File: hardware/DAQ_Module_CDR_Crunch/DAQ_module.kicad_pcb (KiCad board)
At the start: 2 copper layers, 53 parts, among them J1 Conn_01x10_Pin, J2 Conn_01x10_Pin, J3 Conn_01x10_Pin, U1 MCP3564RT-E/ST, U2 MAX31855KASA, U3 MAX31855KASA, U5 TPS70933DBVR, U6 TPS70933DBVR, U7 TPS70933DBVR, U8 MAX31855KASA

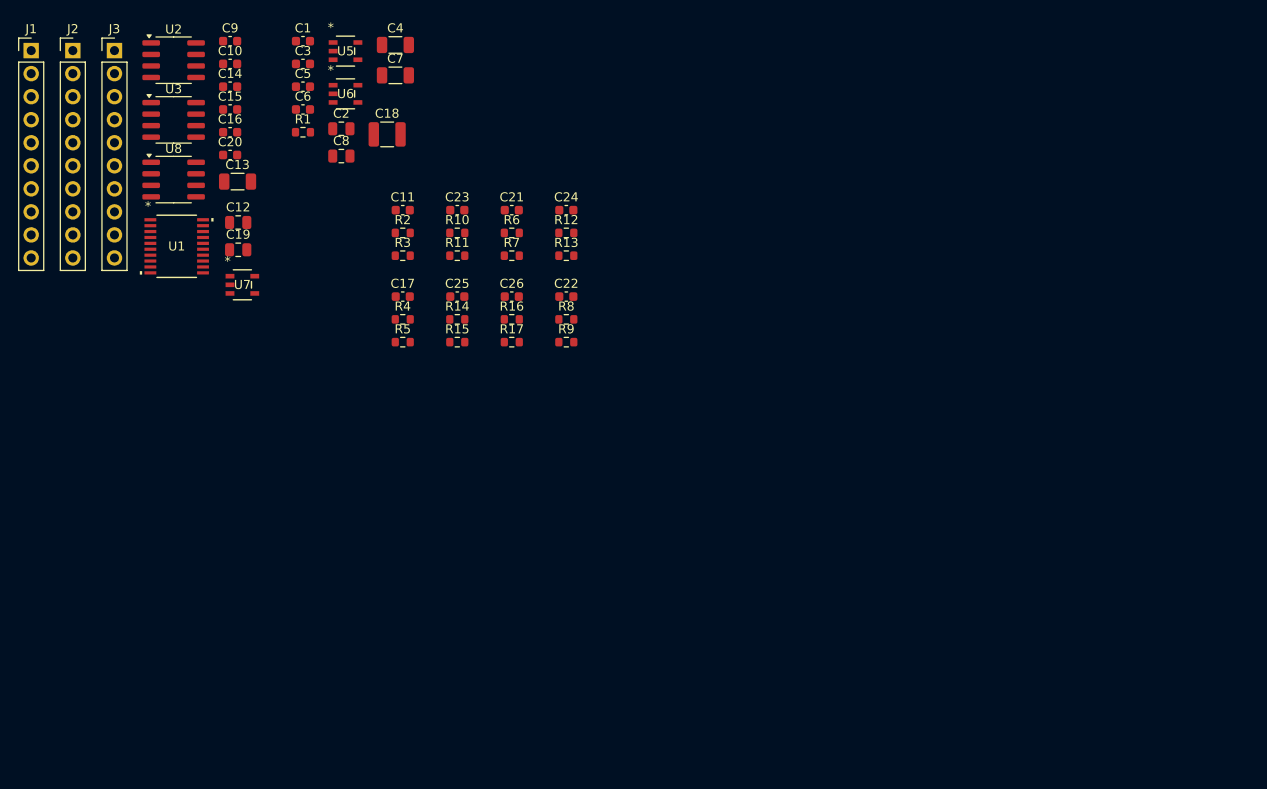
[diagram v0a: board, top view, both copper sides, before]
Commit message: Ready for final review. Added downloadable footprint and symbol of board
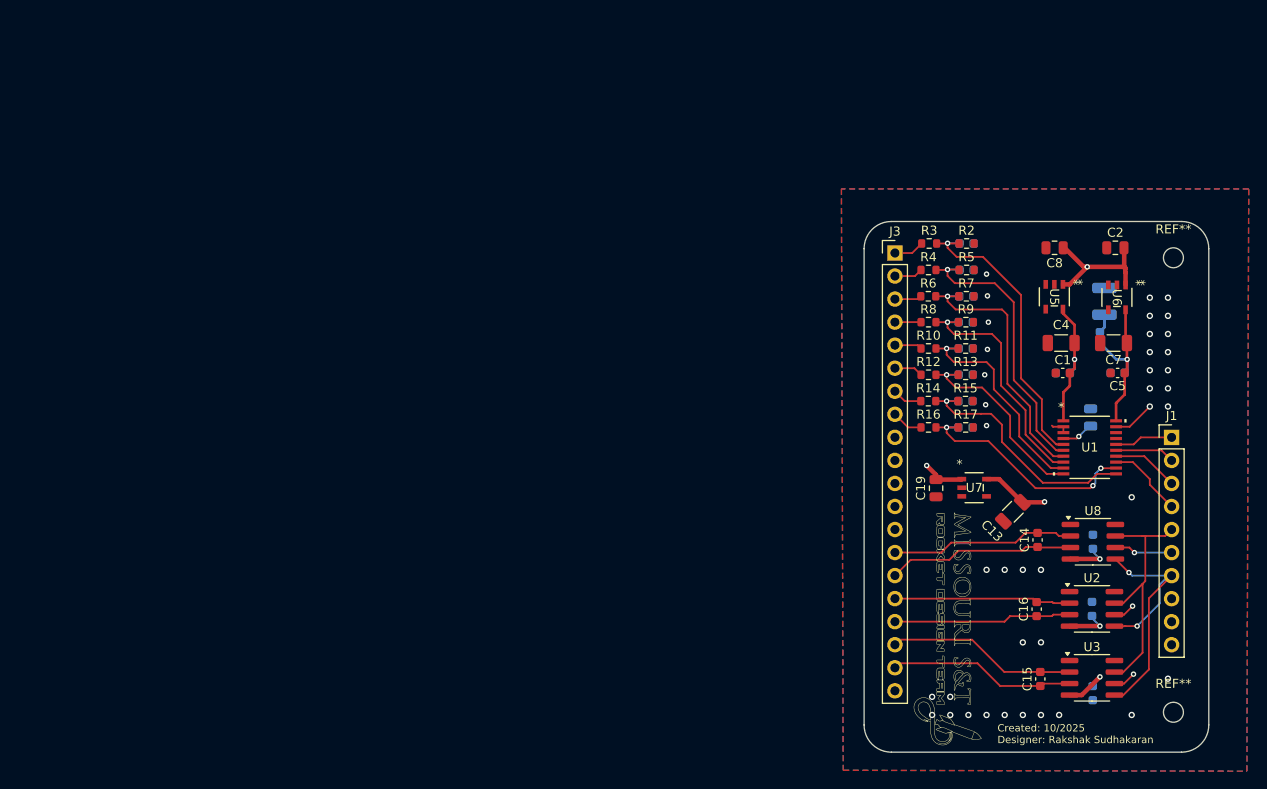
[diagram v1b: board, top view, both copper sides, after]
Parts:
- removed J2: Conn_01x10_Pin, Connector_PinHeader_2.54mm:PinHeader_1x10_P2.54mm_Vertical
- added G***: LOGO, RDT_Logo:RDT_Logo, F.Cu at (169.2, 109.6)
- added REF**: MountingHole_2.2mm_M2, MountingHole:MountingHole_2.2mm_M2, F.Cu at (194.1, 118.8)
- added REF**: MountingHole_2.2mm_M2, MountingHole:MountingHole_2.2mm_M2, F.Cu at (194.1, 68.7)
- C10, C11, C12, C17, C18, C20, C21, C22, C23, C24, C25, C26, C3, C6, C9, R1: moved to B.Cu
- J3: value Conn_01x10_Pin -> Conn_01x20_Pin; footprint Connector_PinHeader_2.54mm:PinHeader_1x10_P2.54mm_Vertical -> Connector_PinHeader_2.54mm:PinHeader_1x20_P2.54mm_Vertical
- moved J1 132.7 mm to (193.9, 88.5)
- moved C9 119.2 mm to (185.2, 116.7), turned to -90 degrees
- moved U3 118.5 mm to (185.1, 115.0)
- moved U2 117.9 mm to (185.1, 107.4)
- moved C10 112.4 mm to (185.1, 107.4), turned to 90 degrees
- moved C15 109.2 mm to (179.4, 115.1), turned to 90 degrees
- moved U8 108.9 mm to (185.2, 100.0)
- moved C20 104.2 mm to (185.2, 100.0), turned to 90 degrees
- moved C16 103.3 mm to (179.0, 107.4), turned to 90 degrees
- moved U1 103.1 mm to (184.9, 89.6)
- moved C14 102.1 mm to (179.1, 99.8), turned to 90 degrees
- moved C12 96.4 mm to (185.0, 86.3), turned to -90 degrees
- moved C5 95.2 mm to (187.9, 81.4), turned to 180 degrees
- moved C6 94.4 mm to (187.9, 81.4), turned to 180 degrees
- moved C13 92.9 mm to (176.4, 96.7), turned to -135 degrees
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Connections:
- C19 pad 1: Net-(U7-GND) -> GND
- C2 pad 1: Net-(U5-GND) -> GND
- C8 pad 2: Net-(U6-GND) -> GND
- J1 pad 2: /GPIO5 (CS_ADC) -> /GPIO7 (MOSI_ADC)
- J1 pad 4: /GPIO7 (MOSI_ADC) -> /GPIO5 (CS_ADC)
- J1 pad 8: /GPIO12 (CS_N20) -> /GPIO13 (CS Chamber Shell_2)
- J1 pad 9: /GPIO13 (CS Chamber Shell_2) -> /GPIO12 (CS_N20)
- J3 pad 1: /T+ (Chamber Shell_1) -> /ADC_AI0
- J3 pad 2: /T- (Chamber Shell_1) -> /ADC_AI1
- J3 pad 3: /T+ (Chamber Shell_2) -> /ADC_AI2
- J3 pad 4: /T- (Chamber Shell_2) -> /ADC_AI3
- J3 pad 5: /T+ (N2O) -> /ADC_AI4
- J3 pad 6: /T- (N2O) -> /ADC_AI5
- J3 pad 7: +5V -> /ADC_AI6
- J3 pad 8: GND -> /ADC_AI7
- U5 pad 2: Net-(U5-GND) -> GND
- U6 pad 2: Net-(U6-GND) -> GND
- U7 pad 2: Net-(U7-GND) -> GND
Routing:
- net +5V: track 0.00 -> 60.7 mm, vias 0 -> 2
- net Net-(U2-V_{CC}): track 0.00 -> 46.8 mm, vias 0 -> 4
- net /ADC_AI_Filt_0: track 0.00 -> 33.5 mm, vias 0 -> 1
- net /GPIO10 (SCK_TCIC): track 0.00 -> 33.1 mm, vias 0 -> 2
- net /ADC_AI_Filt_1: track 0.00 -> 32.2 mm, vias 0 -> 1
- net /ADC_AI_Filt_2: track 0.00 -> 30.5 mm, vias 0 -> 1
- net /ADC_AI_Filt_6: track 0.00 -> 28.0 mm, vias 0 -> 1
- net /GPIO8 (MISO_TCIC): track 0.00 -> 27.8 mm
- net /ADC_AI_Filt_3: track 0.00 -> 27.7 mm, vias 0 -> 1
- net /ADC_AI_Filt_7: track 0.00 -> 27.1 mm, vias 0 -> 3
- net /ADC_AI_Filt_4: track 0.00 -> 25.2 mm, vias 0 -> 1
- net /ADC_AI_Filt_5: track 0.00 -> 22.8 mm, vias 0 -> 1
- net /T- (N2O): track 0.00 -> 21.0 mm
- net /T+ (Chamber Shell_1): track 0.00 -> 20.7 mm
- net /T+ (N2O): track 0.00 -> 20.6 mm
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- added copper zone on B.Cu, net GND
- added copper zone on F.Cu, net GND
- added copper zone on In1.Cu, net GND
- added copper zone on In2.Cu, net GND
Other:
- board outline added: 38 x 58.5 mm
- copper layers 2 -> 4
- board text added: "Created: 10/2025 Designer: Rakshak Sudhakaran"
- board text added: "{ "ViaStitching": "0.2", "stitch_zone_0": { "HSpacing": "1", "VSpacing": "1", "HOffset": "0", "VOffset": "0", "Clearance": "0", "Randomize": false } }"
- board text added: "{ "ViaStitching": "0.2", "stitch_zone_0": { "HSpacing": "1", "VSpacing": "1", "HOffset": "0", "VOffset": "0", "Clearance": "1", "Randomize": false } }"
- board text added: "{ "ViaStitching": "0.2", "stitch_zone_0": { "HSpacing": "1.5", "VSpacing": "1.5", "HOffset": "0", "VOffset": "0", "Clearance": "1.5", "Randomize": false } }"
- board text added: "{ "ViaStitching": "0.2", "stitch_zone_0": { "HSpacing": "2", "VSpacing": "2", "HOffset": "0", "VOffset": "0", "Clearance": "1.5", "Randomize": false } }"
- board text added: "{ "ViaStitching": "0.2", "stitch_zone_0": { "HSpacing": "2", "VSpacing": "2", "HOffset": "0", "VOffset": "0", "Clearance": "1.7", "Randomize": false } }"
- board text added: "{ "ViaStitching": "0.2", "stitch_zone_0": { "HSpacing": "2", "VSpacing": "2", "HOffset": "0", "VOffset": "0", "Clearance": "2", "Randomize": false } }"
- board text added: "{ "ViaStitching": "0.2", "stitch_zone_0": { "HSpacing": "2.5", "VSpacing": "2.5", "HOffset": "0", "VOffset": "0", "Clearance": "2.5", "Randomize": false } }"
- board text added: "{ "ViaStitching": "0.2", "stitch_zone_0": { "HSpacing": "3", "VSpacing": "3", "HOffset": "0", "VOffset": "0", "Clearance": "3", "Randomize": false } }"
- board text added: "{ "ViaStitching": "0.2", "stitch_zone_0": { "HSpacing": "5", "VSpacing": "5", "HOffset": "0", "VOffset": "0", "Clearance": "5", "Randomize": false } }"

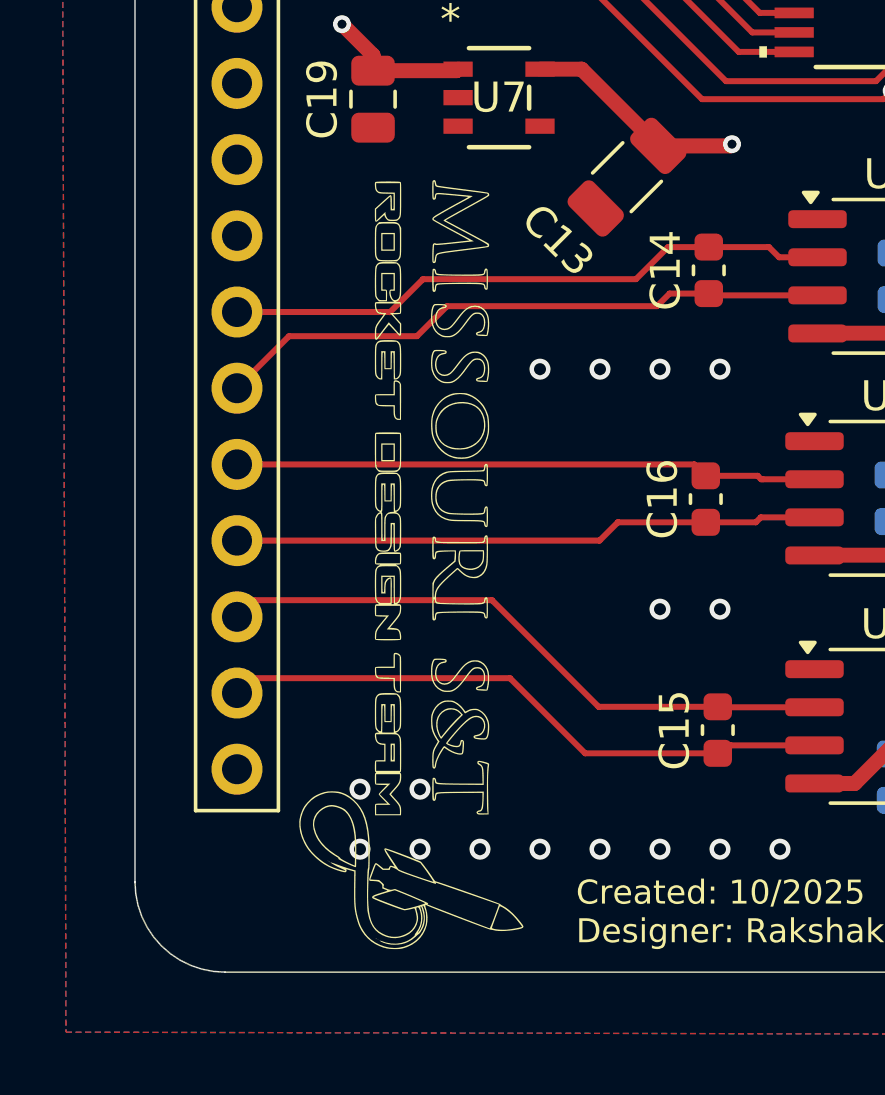
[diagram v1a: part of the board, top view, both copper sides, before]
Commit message: Fixed logo and mounting holes
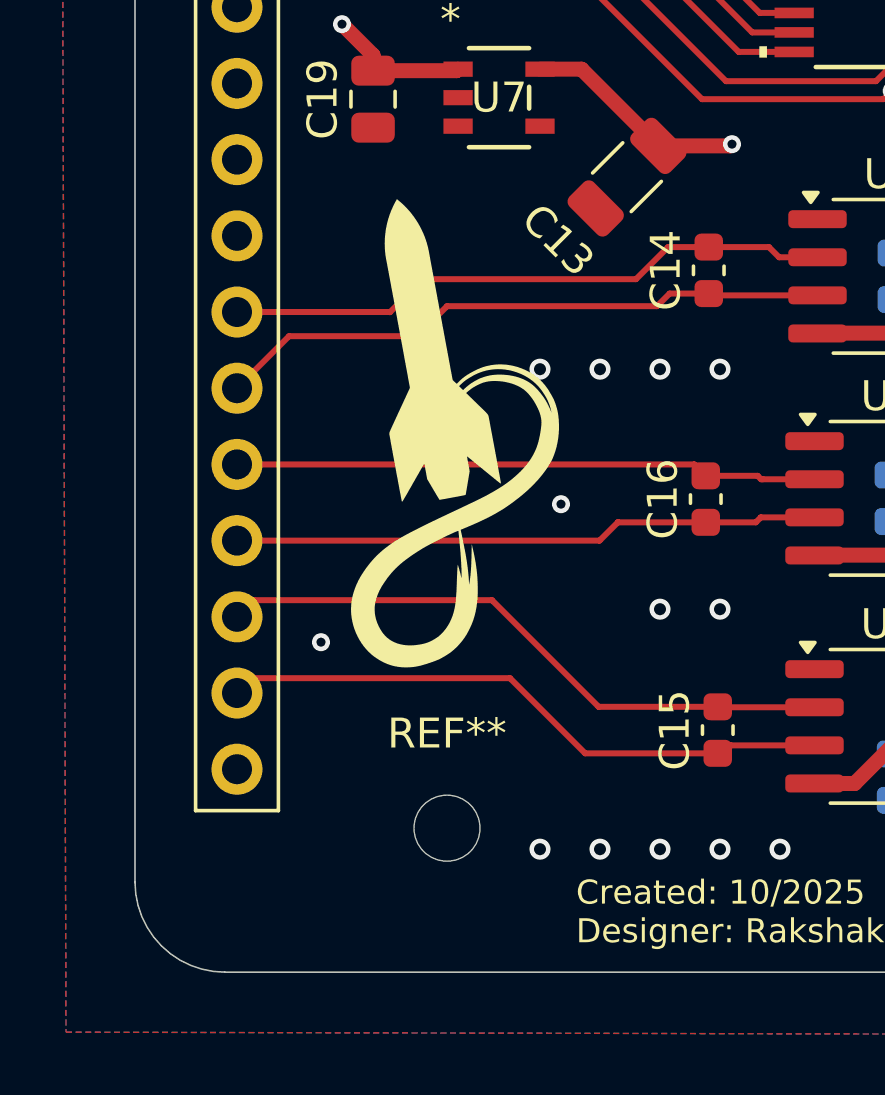
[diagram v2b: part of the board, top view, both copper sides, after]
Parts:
- added REF**: MountingHole_2.2mm_M2, MountingHole:MountingHole_2.2mm_M2, F.Cu at (170.4, 118.4)
- moved G*** 4.30 mm to (169.1, 105.3), turned to 30 degrees
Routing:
- net GND: vias 40 -> 37

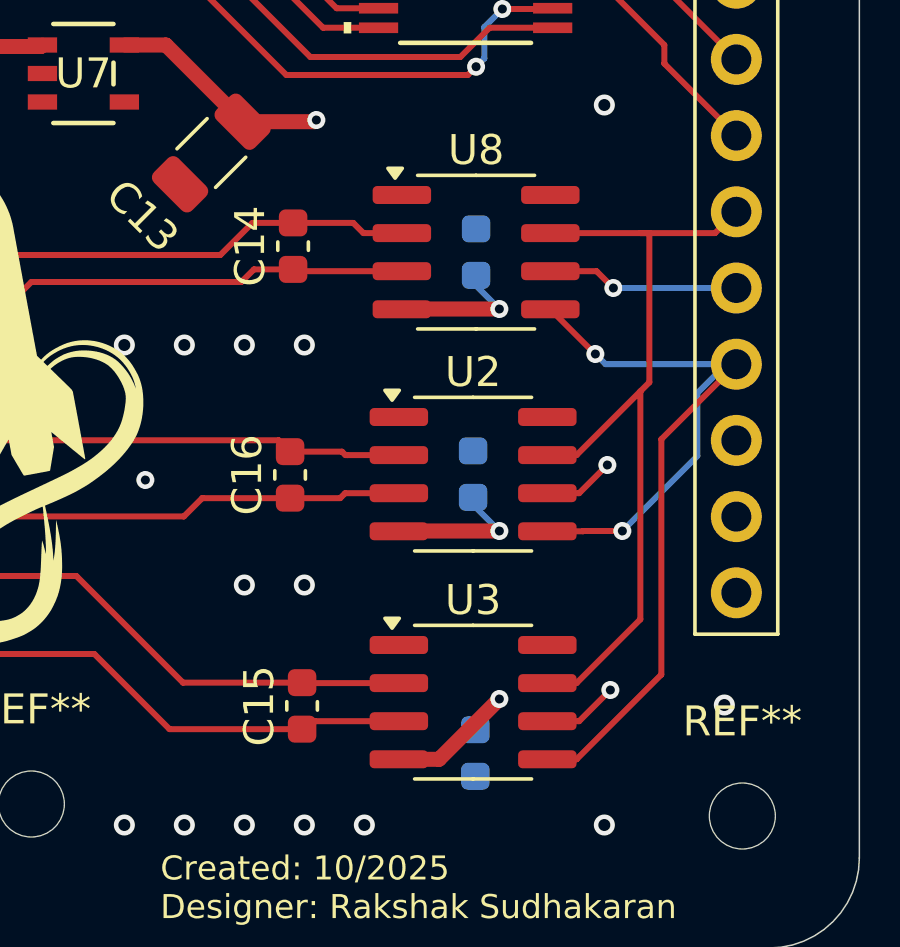
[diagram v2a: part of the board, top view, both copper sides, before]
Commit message: Improved some via spacing
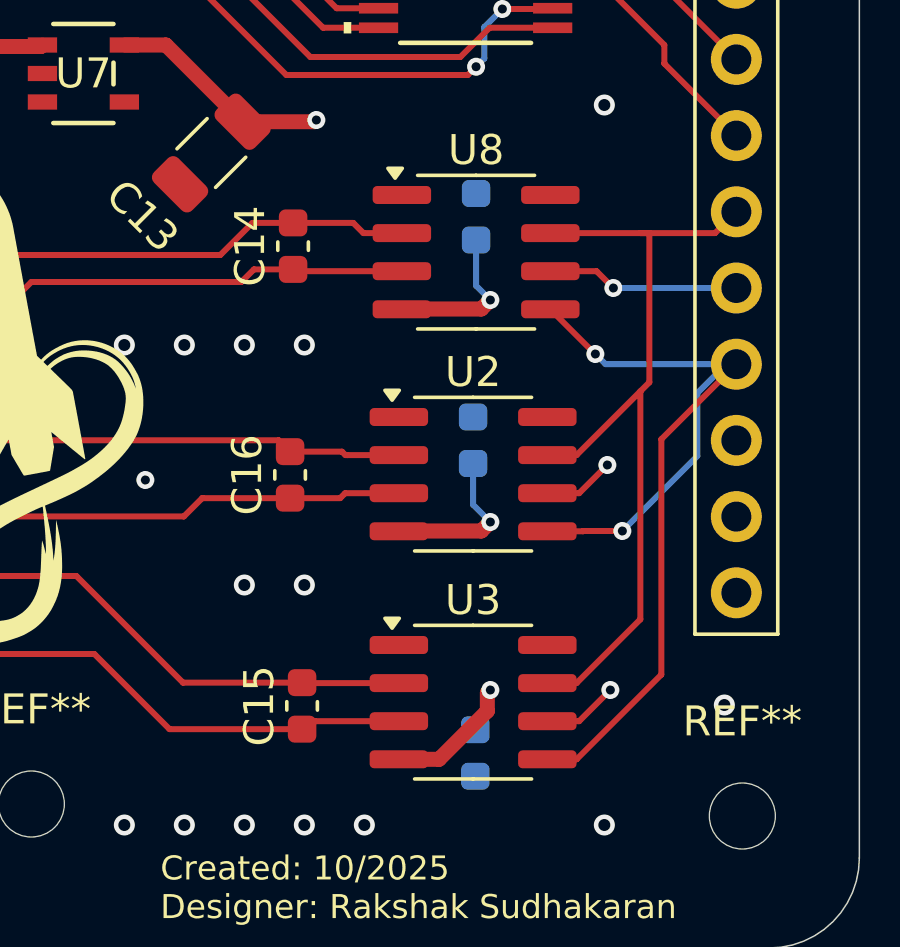
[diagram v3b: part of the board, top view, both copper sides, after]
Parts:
- moved C20 1.18 mm to (185.2, 98.8)
- moved C10 1.13 mm to (185.1, 106.3)
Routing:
- net Net-(U2-V_{CC}): track 46.8 -> 47.9 mm
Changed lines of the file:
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@@
 	(footprint "Capacitor_SMD:C_0603_1608Metric"
 		(layer "B.Cu")
-		(at 185.225 100.005 90)
+		(at 185.225 98.825 90)
 		(descr "Capacitor SMD 0603 (1608 Metric), square (rectangular) end terminal, IPC-7351 nominal, (Body size source: IPC-SM-782 page 76, https://www.pcb-3d.com/wordpress/wp-content/uploads/ipc-sm-782a_amendment_1_and_2.pdf), generated with kicad-footprint-generator")
 		(tags "capacitor")
@@
 	(footprint "Capacitor_SMD:C_0603_1608Metric"
 		(layer "B.Cu")
-		(at 185.125 107.405 90)
+		(at 185.125 106.275 90)
 		(descr "Capacitor SMD 0603 (1608 Metric), square (rectangular) end terminal, IPC-7351 nominal, (Body size source: IPC-SM-782 page 76, https://www.pcb-3d.com/wordpress/wp-content/uploads/ipc-sm-782a_amendment_1_and_2.pdf), generated with kicad-footprint-generator")
 		(tags "capacitor")
@@
 	)
 	(segment
-		(start 186 109.3)
-		(end 182.66 109.3)
+		(start 182.66 109.3)
+		(end 182.65 109.31)
 		(width 0.5)
 		(layer "F.Cu")
@@
 	)
 	(segment
+		(start 185.6 115.3)
+		(end 183.99 116.91)
+		(width 0.5)
+		(layer "F.Cu")
+		(net 5)
+	)
+	(segment
 		(start 174.885964 93.099998)
 		(end 177.442983 95.657017)
@@
 	)
 	(segment
-		(start 186 114.9)
-		(end 183.99 116.91)
+		(start 185.7 109)
+		(end 185.4 109.3)
 		(width 0.5)
 		(layer "F.Cu")
@@
 	)
 	(segment
-		(start 186 101.9)
-		(end 182.76 101.9)
+		(start 185.7 101.6)
+		(end 185.4 101.9)
+		(width 0.5)
+		(layer "F.Cu")
+		(net 5)
+	)
+	(segment
+		(start 185.6 114.7)
+		(end 185.6 115.3)
+		(width 0.5)
+		(layer "F.Cu")
+		(net 5)
+	)
+	(segment
+		(start 183.99 116.91)
+		(end 182.65 116.91)
 		(width 0.5)
 		(layer "F.Cu")
@@
 	)
 	(segment
-		(start 182.66 109.3)
-		(end 182.65 109.31)
+		(start 185.4 109.3)
+		(end 182.66 109.3)
 		(width 0.5)
 		(layer "F.Cu")
@@
 	)
 	(segment
-		(start 183.99 116.91)
-		(end 182.65 116.91)
+		(start 185.7 114.6)
+		(end 185.6 114.7)
+		(width 0.5)
+		(layer "F.Cu")
+		(net 5)
+	)
+	(segment
+		(start 185.4 101.9)
+		(end 182.76 101.9)
 		(width 0.5)
 		(layer "F.Cu")
@@
 	)
 	(via
-		(at 186 114.9)
+		(at 185.7 114.6)
 		(size 0.6)
 		(drill 0.3)
@@
 	)
 	(via
-		(at 186 101.9)
+		(at 185.7 101.6)
 		(size 0.6)
 		(drill 0.3)
@@
 	)
 	(via
-		(at 186 109.3)
+		(at 185.7 109)
 		(size 0.6)
 		(drill 0.3)
@@
 	)
 	(segment
-		(start 185.225 101.125)
-		(end 186 101.9)
+		(start 185.7 114.6)
+		(end 185.6 114.7)
 		(width 0.2)
 		(layer "B.Cu")
@@
 	)
 	(segment
-		(start 185.2 115.925)
-		(end 185.2 115.7)
+		(start 185.6 114.7)
+		(end 185.6 115.3)
 		(width 0.2)
 		(layer "B.Cu")
@@
 	)
 	(segment
-		(start 185.225 100.78)
-		(end 185.225 101.125)
+		(start 185.125 108.425)
+		(end 185.125 107.05)
 		(width 0.2)
 		(layer "B.Cu")
@@
 	)
 	(segment
-		(start 185.125 108.425)
-		(end 186 109.3)
+		(start 185.7 109)
+		(end 185.125 108.425)
 		(width 0.2)
 		(layer "B.Cu")
@@
 	)
 	(segment
-		(start 185.125 108.18)
-		(end 185.125 108.425)
+		(start 185.225 101.125)
+		(end 185.225 99.6)
+		(width 0.2)
+		(layer "B.Cu")
+		(net 5)
+	)
+	(segment
+		(start 185.7 101.6)
+		(end 185.225 101.125)
+		(width 0.2)
+		(layer "B.Cu")
+		(net 5)
+	)
+	(segment
+		(start 185.6 115.3)
+		(end 185.2 115.7)
 		(width 0.2)
 		(layer "B.Cu")
@@
 	(segment
 		(start 185.2 115.7)
-		(end 186 114.9)
+		(end 185.2 115.925)
 		(width 0.2)
 		(layer "B.Cu")
@@
 	)
 	(segment
-		(start 186 109.3)
-		(end 186 114.9)
+		(start 185.7 101.6)
+		(end 185.7 97.2)
 		(width 0.5)
 		(layer "In1.Cu")
@@
 	)
 	(segment
-		(start 186 101.9)
-		(end 186 109.3)
+		(start 185.7 97.2)
+		(end 184.1 95.6)
 		(width 0.5)
 		(layer "In1.Cu")
@@
 	(segment
 		(start 184.1 95.6)
-		(end 186 97.5)
+		(end 179.9 95.6)
 		(width 0.5)
 		(layer "In1.Cu")
@@
 	)
 	(segment
-		(start 179.9 95.6)
-		(end 184.1 95.6)
+		(start 185.7 114.6)
+		(end 185.7 109)
 		(width 0.5)
 		(layer "In1.Cu")
@@
 	)
 	(segment
-		(start 186 97.5)
-		(end 186 101.9)
+		(start 185.7 109)
+		(end 185.7 101.6)
 		(width 0.5)
 		(layer "In1.Cu")
